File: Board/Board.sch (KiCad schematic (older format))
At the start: 38 parts, among them J1 Micro_SD_Card, J2 Conn_01x02_Male, Q1 Q_NMOS_GSD, Q2 Q_NMOS_GSD, SW2 SW_SPST, U1 ATmega328P-AU, U2 TLV61225DCKR, Y1 10MHz

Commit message: First PCB
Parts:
- added C9: 100nF, Capacitor_SMD:C_0603_1608Metric, symbol Device:C
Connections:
- net +3V3: now also C9.1
- net GND: now also C9.2
- net SDGND: no longer names the net of J1.6 (VSS), Q2.2 (S)
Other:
- moved on the sheet: J1, Q2, R6
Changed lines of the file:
@@
 L Connector:Micro_SD_Card J1
 U 1 1 6010CE8A
-P 4700 5400
-F 0 "J1" H 4650 6117 50  0000 C CNN
-F 1 "Micro_SD_Card" H 4650 6026 50  0000 C CNN
-F 2 "Connector_Card:microSD_HC_Wuerth_693072010801" H 5850 5700 50  0001 C CNN
-F 3 "http://katalog.we-online.de/em/datasheet/693072010801.pdf" H 4700 5400 50  0001 C CNN
-	1    4700 5400
-	0    -1   -1   0
+P 4650 5550
+F 0 "J1" H 4600 6267 50  0000 C CNN
+F 1 "Micro_SD_Card" H 4600 6176 50  0000 C CNN
+F 2 "Connector_Card:microSD_HC_Wuerth_693072010801" H 5800 5850 50  0001 C CNN
+F 3 "http://katalog.we-online.de/em/datasheet/693072010801.pdf" H 4650 5550 50  0001 C CNN
+	1    4650 5550
+	-1   0    0    1
 $EndComp
 $Comp
@@
 	1    0    0    -1
 $EndComp
-Text Label 4800 6550 1    50   ~ 0
+Text Label 5800 5450 2    50   ~ 0
 SCK
-Text Label 5000 6550 1    50   ~ 0
+Text Label 5800 5250 2    50   ~ 0
 MISO
-Text Label 4600 6550 1    50   ~ 0
-MOSI
-Text Label 4500 6550 1    50   ~ 0
+Text Label 5800 5750 2    50   ~ 0
 CS
-NoConn ~ 4400 6300
-NoConn ~ 5100 6300
+NoConn ~ 5550 5850
+NoConn ~ 5550 5150
 Wire Wire Line
 	9200 2150 9500 2150
@@
 	0    -1   -1   0
 $EndComp
-NoConn ~ 5300 4600
+NoConn ~ 3850 4950
 $Comp
 L Device:R R4
@@
 	9800 5600 10150 5600
 $Comp
-L Device:Q_NMOS_GSD Q2
-U 1 1 60166A54
-P 5900 6400
-F 0 "Q2" V 6150 6350 50  0000 L CNN
-F 1 "Q_NMOS_GSD" V 6250 6150 50  0000 L CNN
-F 2 "Package_TO_SOT_SMD:SOT-23" H 6100 6500 50  0001 C CNN
-F 3 "~" H 5900 6400 50  0001 C CNN
-	1    5900 6400
-	0    1    1    0
-$EndComp
-$Comp
 L Device:R R6
 U 1 1 60166A5A
-P 5900 6050
-F 0 "R6" H 5700 6100 50  0000 L CNN
-F 1 "1k" H 5700 6000 50  0000 L CNN
-F 2 "Resistor_SMD:R_0603_1608Metric" V 5830 6050 50  0001 C CNN
-F 3 "~" H 5900 6050 50  0001 C CNN
-	1    5900 6050
-	-1   0    0    1
-$EndComp
-Wire Wire Line
-	5900 5500 5900 5900
-Text Label 5900 5500 3    50   ~ 0
+P 5850 6450
+F 0 "R6" V 5650 6400 50  0000 L CNN
+F 1 "1k" V 5750 6400 50  0000 L CNN
+F 2 "Resistor_SMD:R_0603_1608Metric" V 5780 6450 50  0001 C CNN
+F 3 "~" H 5850 6450 50  0001 C CNN
+	1    5850 6450
+	0    1    1    0
+$EndComp
+Wire Wire Line
+	5300 6450 5700 6450
+Text Label 5300 6450 0    50   ~ 0
 SD_POWER
-Text GLabel 5700 6500 0    50   Output ~ 0
-SDGND
-Text GLabel 4900 6550 3    50   Input ~ 0
-SDGND
-Wire Wire Line
-	4500 6300 4500 6550
-Wire Wire Line
-	4600 6300 4600 6550
-Wire Wire Line
-	4700 6300 4700 6550
-Wire Wire Line
-	4800 6300 4800 6550
-Wire Wire Line
-	4900 6300 4900 6550
-Wire Wire Line
-	5000 6300 5000 6550
+Wire Wire Line
+	5550 5750 5800 5750
+Wire Wire Line
+	5550 5650 5800 5650
+Wire Wire Line
+	5550 5450 5800 5450
+Wire Wire Line
+	5550 5250 5800 5250
 Wire Wire Line
 	9200 3850 9650 3850
@@
 Wire Wire Line
 	5350 2750 5350 3100
-$Comp
-L power:+3.3V #PWR0113
-U 1 1 601C51BB
-P 4700 6550
-F 0 "#PWR0113" H 4700 6400 50  0001 C CNN
-F 1 "+3.3V" H 4715 6723 50  0000 C CNN
-F 2 "" H 4700 6550 50  0001 C CNN
-F 3 "" H 4700 6550 50  0001 C CNN
-	1    4700 6550
-	-1   0    0    1
-$EndComp
-$Comp
-L power:GND #PWR0114
-U 1 1 601CA5CE
-P 6100 6500
-F 0 "#PWR0114" H 6100 6250 50  0001 C CNN
-F 1 "GND" V 6105 6372 50  0000 R CNN
-F 2 "" H 6100 6500 50  0001 C CNN
-F 3 "" H 6100 6500 50  0001 C CNN
-	1    6100 6500
-	0    -1   -1   0
-$EndComp
 $Comp
 L Connector:Conn_01x02_Male J2
@@
 Text Notes 10050 3750 0    50   ~ 0
 TX\n
+$Comp
+L Device:C C9
+U 1 1 60216713
+P 6000 5700
+F 0 "C9" V 6150 5800 50  0000 C CNN
+F 1 "100nF" V 6150 5600 50  0000 C CNN
+F 2 "Capacitor_SMD:C_0603_1608Metric" H 6038 5550 50  0001 C CNN
+F 3 "~" H 6000 5700 50  0001 C CNN
+	1    6000 5700
+	1    0    0    -1
+$EndComp
+$Comp
+L power:GND #PWR0103
+U 1 1 60216719
+P 6000 5850
+F 0 "#PWR0103" H 6000 5600 50  0001 C CNN
+F 1 "GND" H 6050 5700 50  0000 R CNN
+F 2 "" H 6000 5850 50  0001 C CNN
+F 3 "" H 6000 5850 50  0001 C CNN
+	1    6000 5850
+	1    0    0    -1
+$EndComp
+$Comp
+L power:GND #PWR0104
+U 1 1 60220953
+P 6300 6650
+F 0 "#PWR0104" H 6300 6400 50  0001 C CNN
+F 1 "GND" H 6350 6500 50  0000 R CNN
+F 2 "" H 6300 6650 50  0001 C CNN
+F 3 "" H 6300 6650 50  0001 C CNN
+	1    6300 6650
+	1    0    0    -1
+$EndComp
+Text Label 5800 5650 2    50   ~ 0
+MOSI
+Wire Wire Line
+	5550 5550 6000 5550
+$Comp
+L power:+3.3V #PWR0105
+U 1 1 6022DD16
+P 6000 5550
+F 0 "#PWR0105" H 6000 5400 50  0001 C CNN
+F 1 "+3.3V" H 6150 5650 50  0000 C CNN
+F 2 "" H 6000 5550 50  0001 C CNN
+F 3 "" H 6000 5550 50  0001 C CNN
+	1    6000 5550
+	1    0    0    -1
+$EndComp
+Connection ~ 6000 5550
+Wire Wire Line
+	6300 5350 6300 6250
+Wire Wire Line
+	5550 5350 6300 5350
+$Comp
+L Device:Q_NMOS_GSD Q2
+U 1 1 60166A54
+P 6200 6450
+F 0 "Q2" V 6450 6400 50  0000 L CNN
+F 1 "Q_NMOS_GSD" V 6550 6200 50  0000 L CNN
+F 2 "Package_TO_SOT_SMD:SOT-23" H 6400 6550 50  0001 C CNN
+F 3 "~" H 6200 6450 50  0001 C CNN
+	1    6200 6450
+	1    0    0    1
+$EndComp
 $EndSCHEMATC

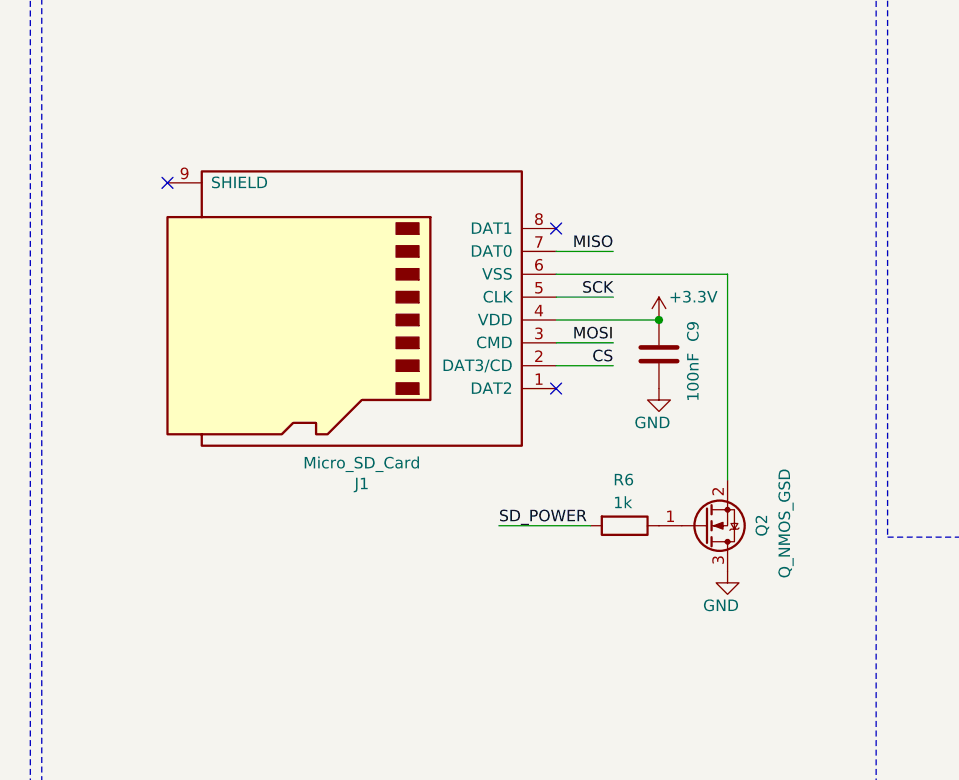
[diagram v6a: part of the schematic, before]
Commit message: Replaced SD connector by correct one
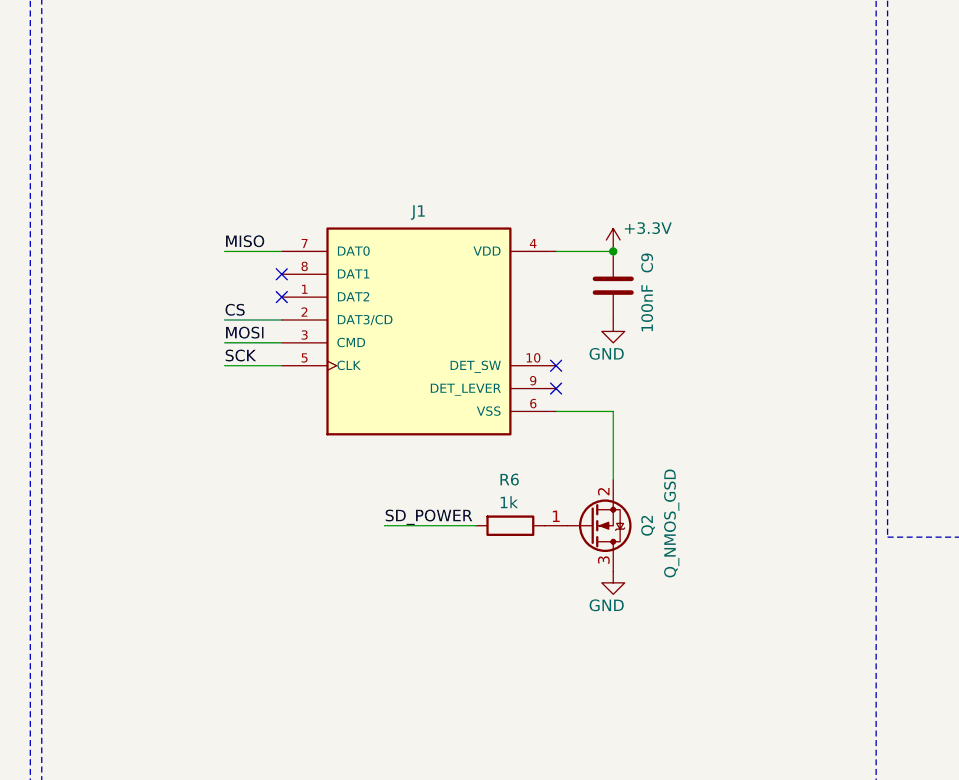
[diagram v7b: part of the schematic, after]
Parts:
- removed J1: Micro_SD_Card, Connector_Card:microSD_HC_Wuerth_693072010801, symbol Connector:Micro_SD_Card
- added J1: 5025700893, Board:MOLEX_5025700893, symbol Symbols:5025700893
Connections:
- net +3V3: now also J1.4 (VDD)
- net CS: now also J1.2 (DAT3/CD)
- net MISO: now also J1.7 (DAT0)
- net MOSI: now also J1.3 (CMD)
- net SCK: now also J1.5 (CLK)
- net at Q2.2 (S): now also J1.6 (VSS)
- no-connect marks 12 -> 13
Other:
- moved on the sheet: C9, Q2, R6
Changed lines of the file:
@@
 $EndDescr
-$Comp
-L Connector:Micro_SD_Card J1
-U 1 1 6010CE8A
-P 4650 5550
-F 0 "J1" H 4600 6267 50  0000 C CNN
-F 1 "Micro_SD_Card" H 4600 6176 50  0000 C CNN
-F 2 "Connector_Card:microSD_HC_Wuerth_693072010801" H 5800 5850 50  0001 C CNN
-F 3 "http://katalog.we-online.de/em/datasheet/693072010801.pdf" H 4650 5550 50  0001 C CNN
-	1    4650 5550
-	-1   0    0    1
-$EndComp
 $Comp
 L Device:Speaker LS1
@@
 	1    0    0    -1
 $EndComp
-Text Label 5800 5450 2    50   ~ 0
+Text Label 4100 5750 0    50   ~ 0
 SCK
-Text Label 5800 5250 2    50   ~ 0
+Text Label 4100 5250 0    50   ~ 0
 MISO
-Text Label 5800 5750 2    50   ~ 0
+Text Label 4100 5550 0    50   ~ 0
 CS
-NoConn ~ 5550 5850
-NoConn ~ 5550 5150
 Wire Wire Line
 	9200 2150 9500 2150
@@
 	0    -1   -1   0
 $EndComp
-NoConn ~ 3850 4950
 $Comp
 L Device:R R4
@@
 L Device:R R6
 U 1 1 60166A5A
-P 5850 6450
-F 0 "R6" V 5650 6400 50  0000 L CNN
-F 1 "1k" V 5750 6400 50  0000 L CNN
-F 2 "Resistor_SMD:R_0603_1608Metric" V 5780 6450 50  0001 C CNN
-F 3 "~" H 5850 6450 50  0001 C CNN
-	1    5850 6450
-	0    1    1    0
-$EndComp
-Wire Wire Line
-	5300 6450 5700 6450
-Text Label 5300 6450 0    50   ~ 0
+P 5350 6450
+F 0 "R6" V 5150 6400 50  0000 L CNN
+F 1 "1k" V 5250 6400 50  0000 L CNN
+F 2 "Resistor_SMD:R_0603_1608Metric" V 5280 6450 50  0001 C CNN
+F 3 "~" H 5350 6450 50  0001 C CNN
+	1    5350 6450
+	0    1    1    0
+$EndComp
+Wire Wire Line
+	4800 6450 5200 6450
+Text Label 4800 6450 0    50   ~ 0
 SD_POWER
 Wire Wire Line
-	5550 5750 5800 5750
-Wire Wire Line
-	5550 5650 5800 5650
-Wire Wire Line
-	5550 5450 5800 5450
-Wire Wire Line
-	5550 5250 5800 5250
+	4350 5550 4100 5550
+Wire Wire Line
+	4350 5650 4100 5650
+Wire Wire Line
+	4350 5750 4100 5750
+Wire Wire Line
+	4350 5250 4100 5250
 Wire Wire Line
 	9200 3850 9650 3850
@@
 TX\n
 $Comp
-L Device:C C9
-U 1 1 60216713
-P 6000 5700
-F 0 "C9" V 6150 5800 50  0000 C CNN
-F 1 "100nF" V 6150 5600 50  0000 C CNN
-F 2 "Capacitor_SMD:C_0603_1608Metric" H 6038 5550 50  0001 C CNN
-F 3 "~" H 6000 5700 50  0001 C CNN
-	1    6000 5700
-	1    0    0    -1
-$EndComp
-$Comp
-L power:GND #PWR0103
-U 1 1 60216719
-P 6000 5850
-F 0 "#PWR0103" H 6000 5600 50  0001 C CNN
-F 1 "GND" H 6050 5700 50  0000 R CNN
-F 2 "" H 6000 5850 50  0001 C CNN
-F 3 "" H 6000 5850 50  0001 C CNN
-	1    6000 5850
-	1    0    0    -1
-$EndComp
-$Comp
 L power:GND #PWR0104
 U 1 1 60220953
-P 6300 6650
-F 0 "#PWR0104" H 6300 6400 50  0001 C CNN
-F 1 "GND" H 6350 6500 50  0000 R CNN
-F 2 "" H 6300 6650 50  0001 C CNN
-F 3 "" H 6300 6650 50  0001 C CNN
-	1    6300 6650
-	1    0    0    -1
-$EndComp
-Text Label 5800 5650 2    50   ~ 0
+P 5800 6650
+F 0 "#PWR0104" H 5800 6400 50  0001 C CNN
+F 1 "GND" H 5850 6500 50  0000 R CNN
+F 2 "" H 5800 6650 50  0001 C CNN
+F 3 "" H 5800 6650 50  0001 C CNN
+	1    5800 6650
+	1    0    0    -1
+$EndComp
+Text Label 4100 5650 0    50   ~ 0
 MOSI
-Wire Wire Line
-	5550 5550 6000 5550
-$Comp
-L power:+3.3V #PWR0105
-U 1 1 6022DD16
-P 6000 5550
-F 0 "#PWR0105" H 6000 5400 50  0001 C CNN
-F 1 "+3.3V" H 6150 5650 50  0000 C CNN
-F 2 "" H 6000 5550 50  0001 C CNN
-F 3 "" H 6000 5550 50  0001 C CNN
-	1    6000 5550
-	1    0    0    -1
-$EndComp
-Connection ~ 6000 5550
-Wire Wire Line
-	6300 5350 6300 6250
-Wire Wire Line
-	5550 5350 6300 5350
 $Comp
 L Device:Q_NMOS_GSD Q2
 U 1 1 60166A54
-P 6200 6450
-F 0 "Q2" V 6450 6400 50  0000 L CNN
-F 1 "Q_NMOS_GSD" V 6550 6200 50  0000 L CNN
-F 2 "Package_TO_SOT_SMD:SOT-23" H 6400 6550 50  0001 C CNN
-F 3 "~" H 6200 6450 50  0001 C CNN
-	1    6200 6450
+P 5700 6450
+F 0 "Q2" V 5950 6400 50  0000 L CNN
+F 1 "Q_NMOS_GSD" V 6050 6200 50  0000 L CNN
+F 2 "Package_TO_SOT_SMD:SOT-23" H 5900 6550 50  0001 C CNN
+F 3 "~" H 5700 6450 50  0001 C CNN
+	1    5700 6450
 	1    0    0    1
 $EndComp
@@
 Text GLabel 10150 4250 0    50   Input ~ 0
 MCU_POWER
+$Comp
+L Symbols:5025700893 J1
+U 1 1 6023787B
+P 4950 5550
+F 0 "J1" H 4950 6025 50  0000 C CNN
+F 1 "5025700893" H 4750 4950 50  0001 L BNN
+F 2 "Board:MOLEX_5025700893" H 4600 4850 50  0001 L BNN
+F 3 "" H 4950 5550 50  0001 L BNN
+F 4 "Molex" H 4950 5550 50  0001 L BNN "MANUFACTURER"
+	1    4950 5550
+	1    0    0    -1
+$EndComp
+$Comp
+L power:+3.3V #PWR0105
+U 1 1 6022DD16
+P 5800 5250
+F 0 "#PWR0105" H 5800 5100 50  0001 C CNN
+F 1 "+3.3V" H 5950 5350 50  0000 C CNN
+F 2 "" H 5800 5250 50  0001 C CNN
+F 3 "" H 5800 5250 50  0001 C CNN
+	1    5800 5250
+	1    0    0    -1
+$EndComp
+$Comp
+L power:GND #PWR0103
+U 1 1 60216719
+P 5800 5550
+F 0 "#PWR0103" H 5800 5300 50  0001 C CNN
+F 1 "GND" H 5850 5400 50  0000 R CNN
+F 2 "" H 5800 5550 50  0001 C CNN
+F 3 "" H 5800 5550 50  0001 C CNN
+	1    5800 5550
+	1    0    0    -1
+$EndComp
+$Comp
+L Device:C C9
+U 1 1 60216713
+P 5800 5400
+F 0 "C9" V 5950 5500 50  0000 C CNN
+F 1 "100nF" V 5950 5300 50  0000 C CNN
+F 2 "Capacitor_SMD:C_0603_1608Metric" H 5838 5250 50  0001 C CNN
+F 3 "~" H 5800 5400 50  0001 C CNN
+	1    5800 5400
+	1    0    0    -1
+$EndComp
+Wire Wire Line
+	5550 5250 5800 5250
+Connection ~ 5800 5250
+NoConn ~ 5550 5750
+NoConn ~ 5550 5850
+Wire Wire Line
+	5550 5950 5800 5950
+Wire Wire Line
+	5800 5950 5800 6250
+NoConn ~ 4350 5450
+NoConn ~ 4350 5350
 $EndSCHEMATC

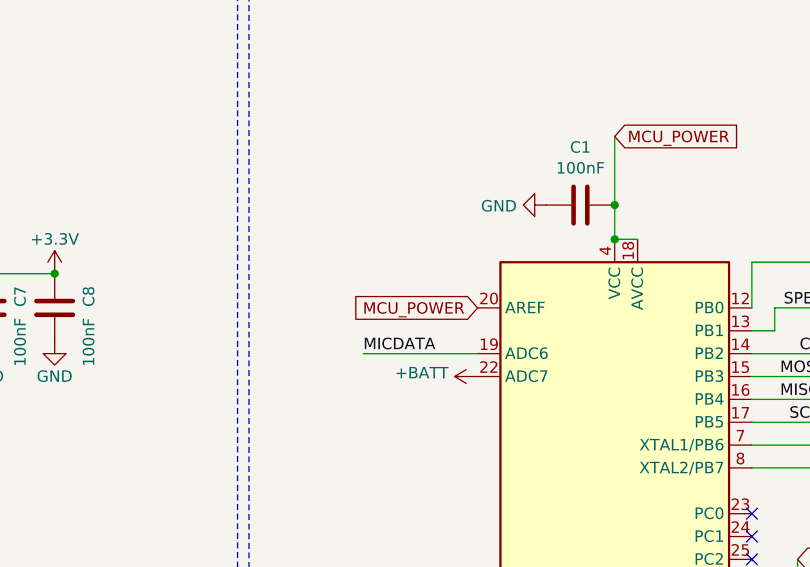
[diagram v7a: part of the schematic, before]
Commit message: Board V1.1: ARef fix
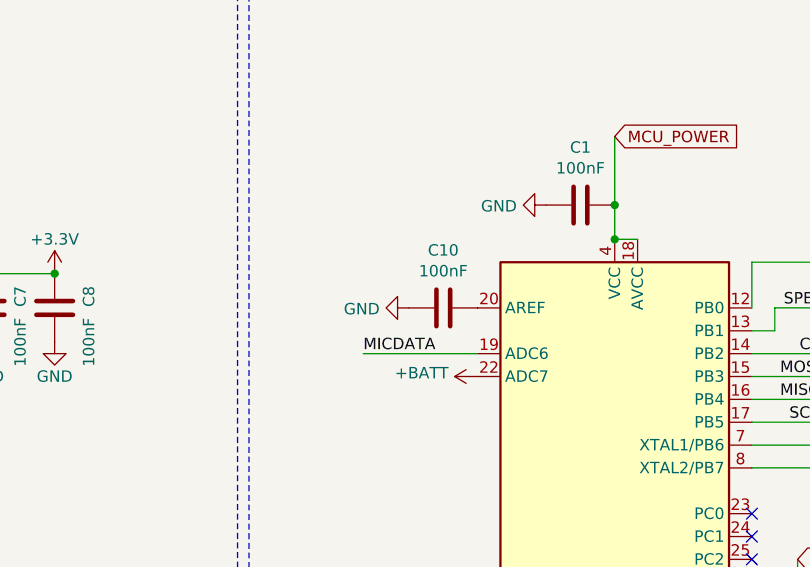
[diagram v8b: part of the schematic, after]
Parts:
- added C10: 100nF, Capacitor_SMD:C_0603_1608Metric, symbol Device:C
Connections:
- net +5V: no longer U1.20 (AREF)
- net GND: now also C10.2
- new net: C10.1, U1.20 (AREF)
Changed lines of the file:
@@
 Sheet 1 1
 Title "Hen translator"
-Date "2021-01-26"
-Rev "V1.0"
+Date "2021-03-10"
+Rev "V1.1"
 Comp ""
 Comment1 ""
@@
 Text GLabel 9400 3050 2    50   Input ~ 0
 MCU_POWER
-Text GLabel 8000 1950 0    50   Input ~ 0
-MCU_POWER
 Text GLabel 8600 1200 2    50   Input ~ 0
 MCU_POWER
@@
 NoConn ~ 4350 5450
 NoConn ~ 4350 5350
+$Comp
+L Device:C C10
+U 1 1 60491239
+P 7850 1950
+F 0 "C10" V 7598 1950 50  0000 C CNN
+F 1 "100nF" V 7689 1950 50  0000 C CNN
+F 2 "Capacitor_SMD:C_0603_1608Metric" H 7888 1800 50  0001 C CNN
+F 3 "~" H 7850 1950 50  0001 C CNN
+	1    7850 1950
+	0    1    1    0
+$EndComp
+$Comp
+L power:GND #PWR015
+U 1 1 6049123F
+P 7700 1950
+F 0 "#PWR015" H 7700 1700 50  0001 C CNN
+F 1 "GND" V 7705 1822 50  0000 R CNN
+F 2 "" H 7700 1950 50  0001 C CNN
+F 3 "" H 7700 1950 50  0001 C CNN
+	1    7700 1950
+	0    1    1    0
+$EndComp
 $EndSCHEMATC
